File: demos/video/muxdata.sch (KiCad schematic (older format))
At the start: 5 parts, among them U22 XC4003-VQ100, U3 74LS245, U4 74LS245, U5 74LS245, U6 74LS245

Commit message: Pcbnew: Minor fix in hotkeys. Demos: add an example to use  a local fp-lib-table and local libs, and update schematics and boards.
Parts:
- U22: footprint (none) -> lib_smd:VQFP100
- U3, U4, U5, U6: footprint (none) -> lib_smd:SO20L
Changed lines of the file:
@@
-EESchema Schematic File Version 2  date 18/11/2010 18:50:34
+EESchema Schematic File Version 2
 LIBS:power
 LIBS:device
@@
 LIBS:xilinx
 LIBS:special
-LIBS:microcontrollers
-LIBS:dsp
-LIBS:microchip
 LIBS:analog_switches
 LIBS:motorola
-LIBS:texas
 LIBS:intel
 LIBS:audio
 LIBS:interface
-LIBS:digital-audio
 LIBS:philips
-LIBS:display
 LIBS:cypress
 LIBS:siliconi
-LIBS:opto
-LIBS:atmel
-LIBS:contrib
-LIBS:valves
 LIBS:video-cache
-EELAYER 24  0
+EELAYER 24 0
 EELAYER END
-$Descr A4 11700 8267
+$Descr A4 11693 8268
+encoding utf-8
 Sheet 2 8
 Title "Video"
@@
 F 0 "U6" H 2250 4700 60  0000 C CNN
 F 1 "74LS245" H 2250 4600 60  0000 C CNN
+F 2 "lib_smd:SO20L" H 2250 4900 60  0001 C CNN
+F 3 "" H 2250 4900 60  0001 C CNN
 	1    2250 4900
 	1    0    0    -1
@@
 F 0 "U5" H 2250 3500 60  0000 C CNN
 F 1 "74LS245" H 2250 3400 60  0000 C CNN
+F 2 "lib_smd:SO20L" H 2250 3700 60  0001 C CNN
+F 3 "" H 2250 3700 60  0001 C CNN
 	1    2250 3700
 	1    0    0    -1
@@
 F 0 "U4" H 2250 2300 60  0000 C CNN
 F 1 "74LS245" H 2250 2200 60  0000 C CNN
+F 2 "lib_smd:SO20L" H 2250 2500 60  0001 C CNN
+F 3 "" H 2250 2500 60  0001 C CNN
 	1    2250 2500
 	1    0    0    -1
@@
 F 0 "U3" H 2250 1100 60  0000 C CNN
 F 1 "74LS245" H 2250 1000 60  0000 C CNN
+F 2 "lib_smd:SO20L" H 2250 1300 60  0001 C CNN
+F 3 "" H 2250 1300 60  0001 C CNN
 	1    2250 1300
 	1    0    0    -1
@@
 F 0 "#PWR06" H 5050 1450 40  0001 C CNN
 F 1 "VCC" H 5050 1400 40  0000 C CNN
+F 2 "" H 5050 1250 60  0001 C CNN
+F 3 "" H 5050 1250 60  0001 C CNN
 	1    5050 1250
 	1    0    0    -1
@@
 F 0 "U22" H 6000 3650 70  0000 C CNN
 F 1 "XC4003-VQ100" H 6000 3450 70  0000 C CNN
+F 2 "lib_smd:VQFP100" H 6000 3550 60  0001 C CNN
+F 3 "" H 6000 3550 60  0001 C CNN
 	1    6000 3550
 	1    0    0    -1

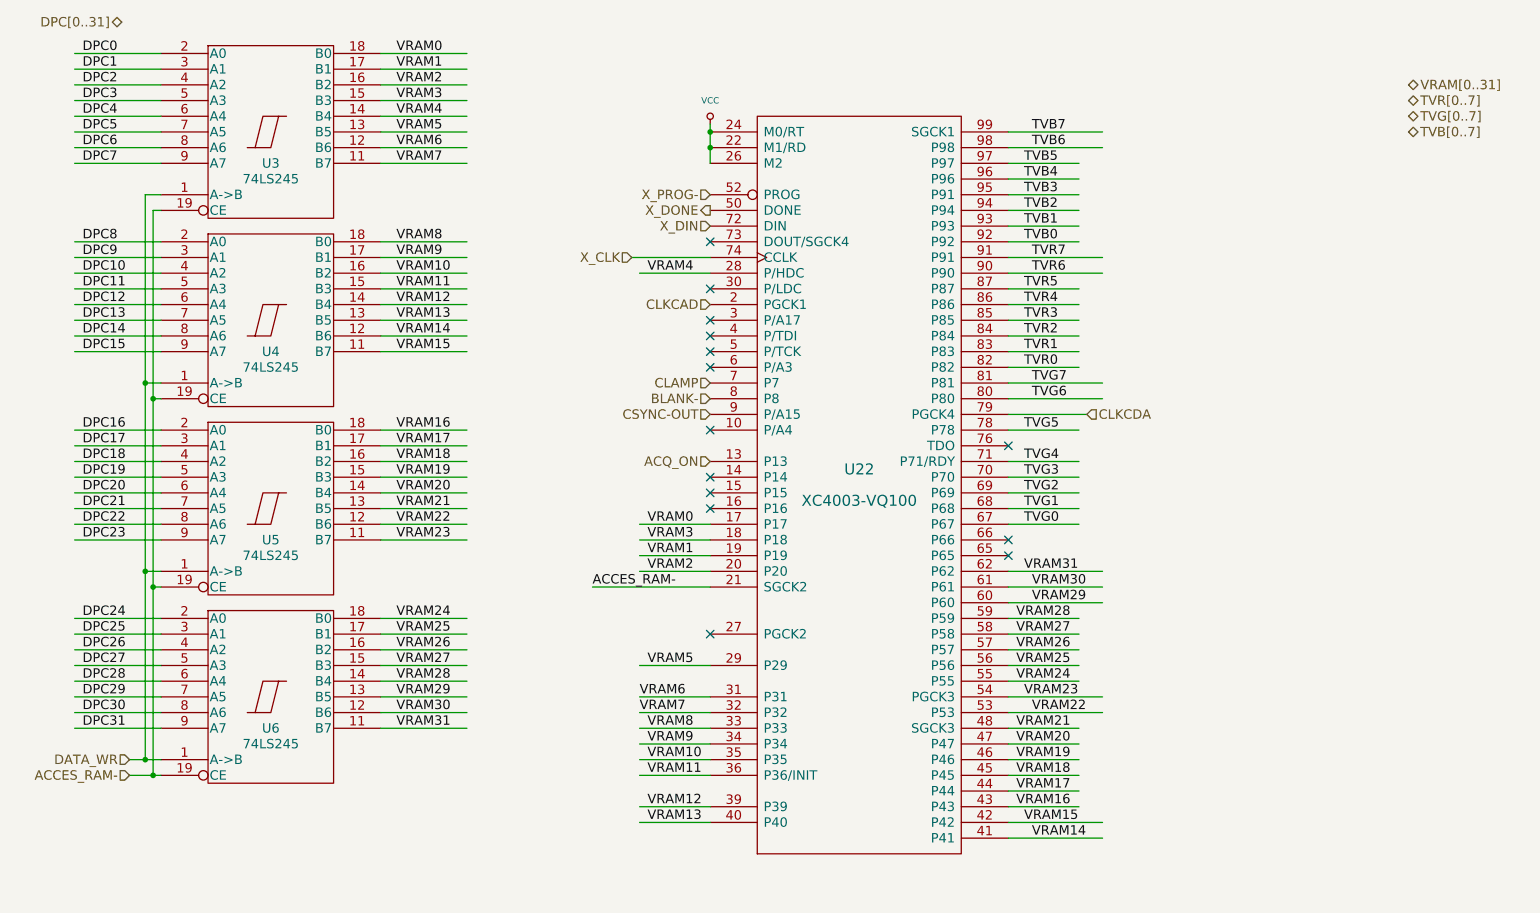
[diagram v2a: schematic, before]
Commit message: demos/ schematic tidying
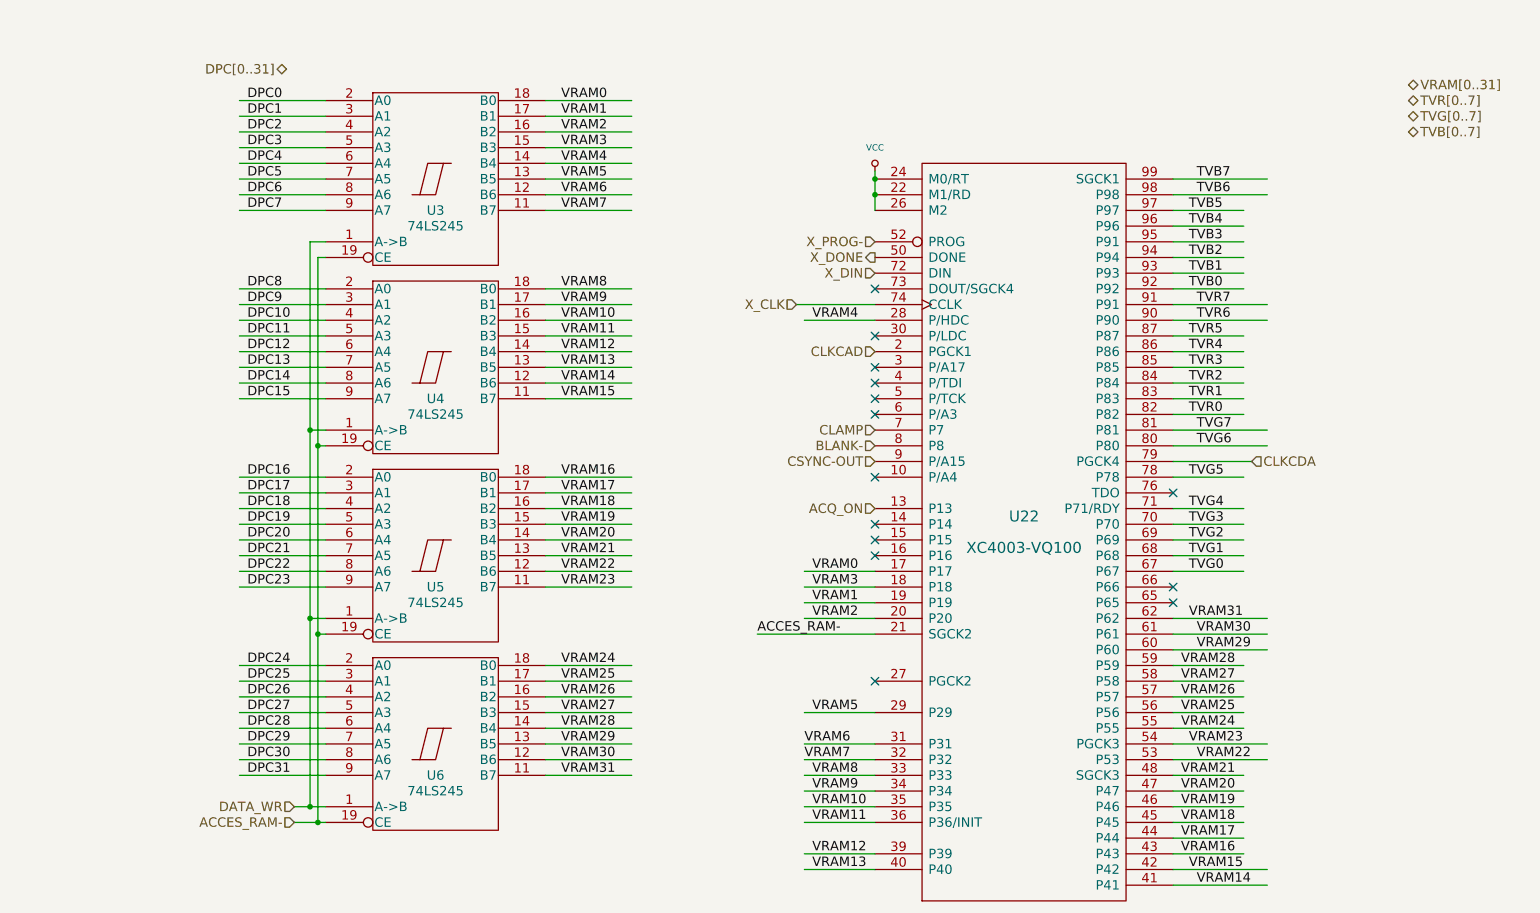
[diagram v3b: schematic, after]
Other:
- moved on the sheet: U22, U3, U4, U5, U6
